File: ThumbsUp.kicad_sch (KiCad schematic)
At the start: 34 parts, among them J10 Raiser_Male, J13 Raiser_Female, J14 Raiser_Male, J17 Raiser_Female, J18 Raiser_Male, J19 Raiser_Female, J24 Conn_01x04_Male, J26 Conn_01x04_Male, J28 Conn_01x04_Female, J30 Conn_01x04_Female, J33 Raiser_Male, J34 Raiser_Female, J35 Raiser_Male, J38 Raiser_Female, J39 Raiser_Male, J40 Raiser_Female, J41 Raiser_Male, J47 Raiser_Female, J48 Raiser_Male, J9 Raiser_Female

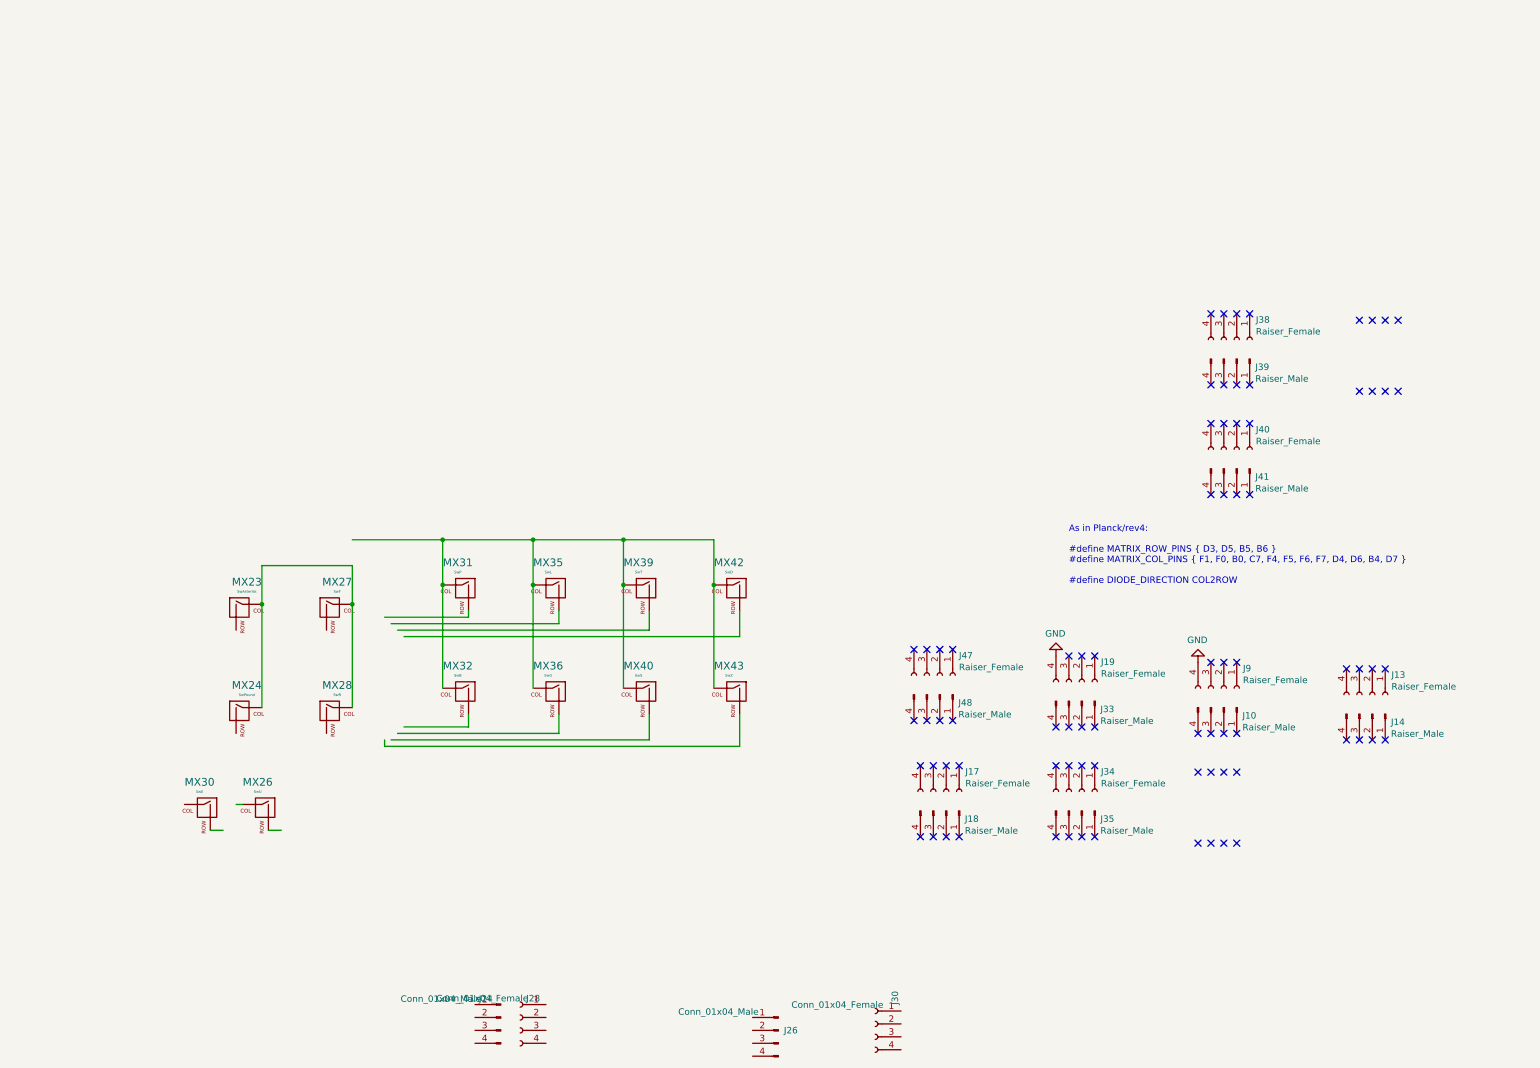
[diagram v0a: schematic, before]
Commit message: K12: Draft schematics, initial physical layout.
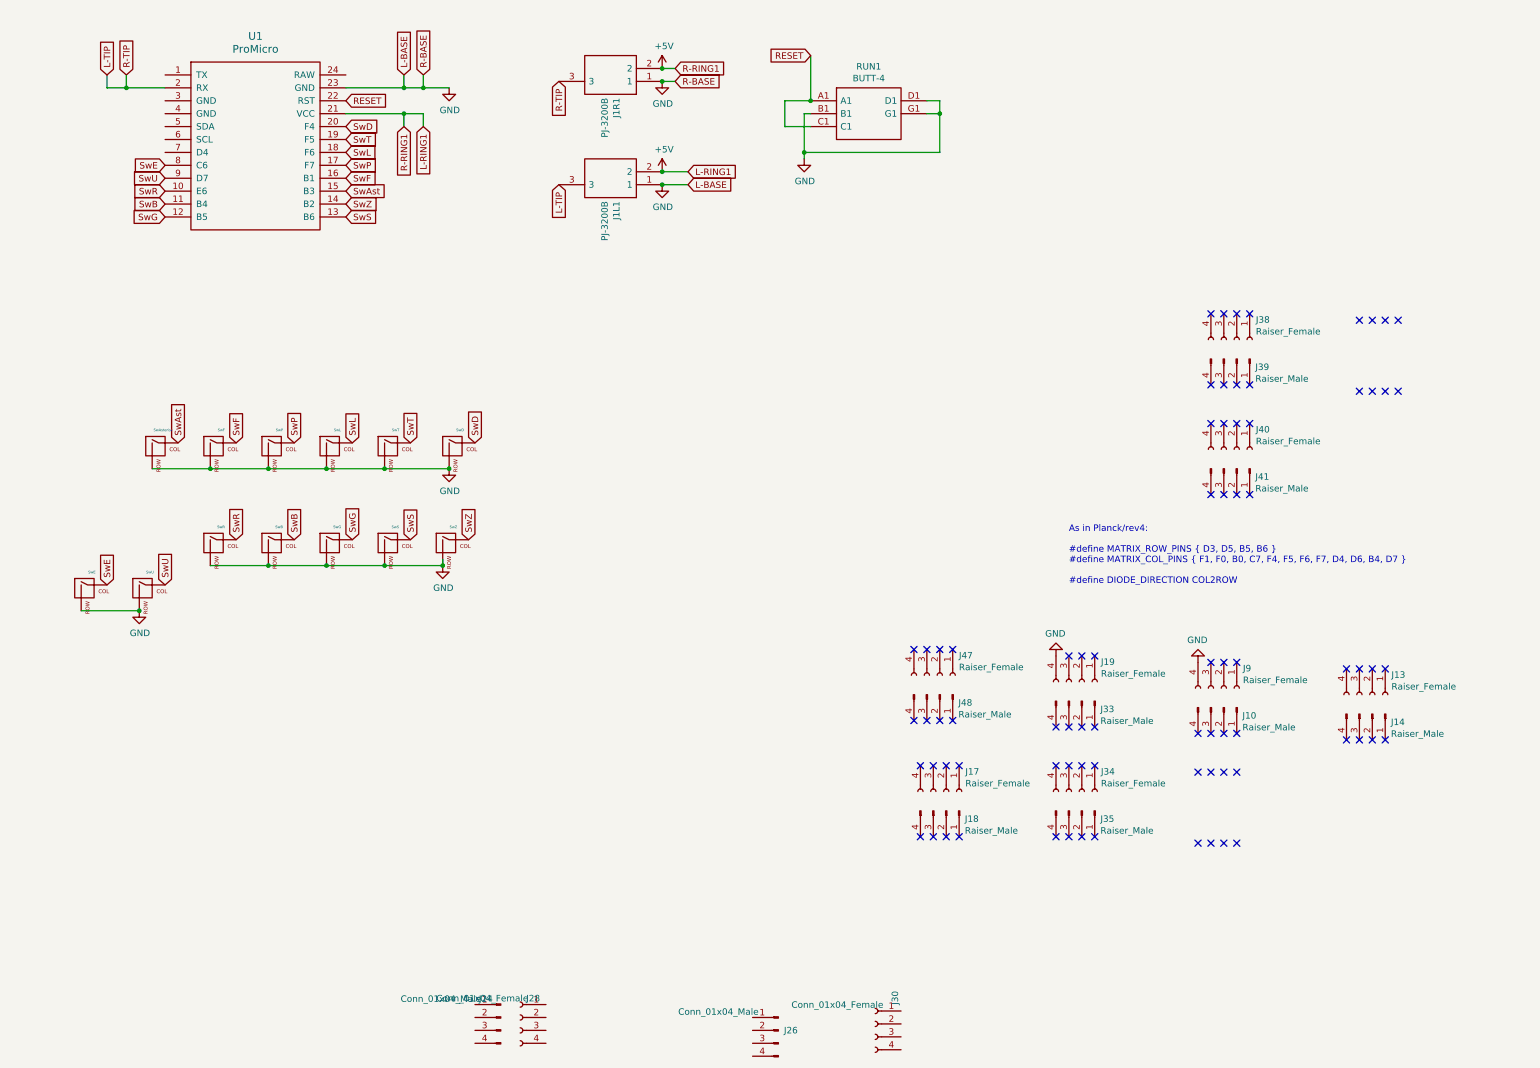
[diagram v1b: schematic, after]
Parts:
- removed MX24: SwPound, footprints:SW_D2FC_OMR, symbol ThumbsUp-rescue:MX-NoLED-MX_Alps_Hybrid
- added J1L1, J1R1: PJ-3200B, random-keyboard-parts:PJ-3200B-4A, symbol STX-3501-3N:STX-3501-3N
- added RUN1: BUTT-4, KiCad:BUTT4, symbol BUTT-4:BUTT-4
- added U1: ProMicro, promicro:ProMicro-NoSilk, symbol promicro:ProMicro
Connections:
- net GND: now also MX23.2 (ROW), MX26.2 (ROW), MX27.2 (ROW), MX28.2 (ROW), MX30.2 (ROW), MX31.2 (ROW), MX32.2 (ROW), MX35.2 (ROW), MX36.2 (ROW), MX39.2 (ROW), MX40.2 (ROW), MX42.2 (ROW), MX43.2 (ROW), J1L1.1, J1R1.1, RUN1.B1, RUN1.D1, RUN1.G1, U1.23 (GND)
- net SwE: now reaches MX30.1 (COL)
- net SwE: now also U1.8 (C6)
- net SwU: now reaches MX26.1 (COL)
- net SwU: now also U1.9 (D7)
- new net +5V: J1L1.2, J1R1.2, U1.21 (VCC)
- new net L-TIP: J1L1.3, J1R1.3, U1.2 (RX)
- new net RESET: RUN1.A1, RUN1.C1, U1.22 (RST)
- new net SwAst: MX23.1 (COL), U1.15 (B3)
- new net SwB: MX32.1 (COL), U1.11 (B4)
- new net SwD: MX42.1 (COL), U1.20 (F4)
- new net SwF: MX27.1 (COL), U1.16 (B1)
- new net SwG: MX36.1 (COL), U1.12 (B5)
- new net SwL: MX35.1 (COL), U1.18 (F6)
- new net SwP: MX31.1 (COL), U1.17 (F7)
- new net SwR: MX28.1 (COL), U1.10 (E6)
- new net SwS: MX40.1 (COL), U1.13 (B6)
- new net SwT: MX39.1 (COL), U1.19 (F5)
- new net SwZ: MX43.1 (COL), U1.14 (B2)

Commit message: K12: Before splitting the boards.
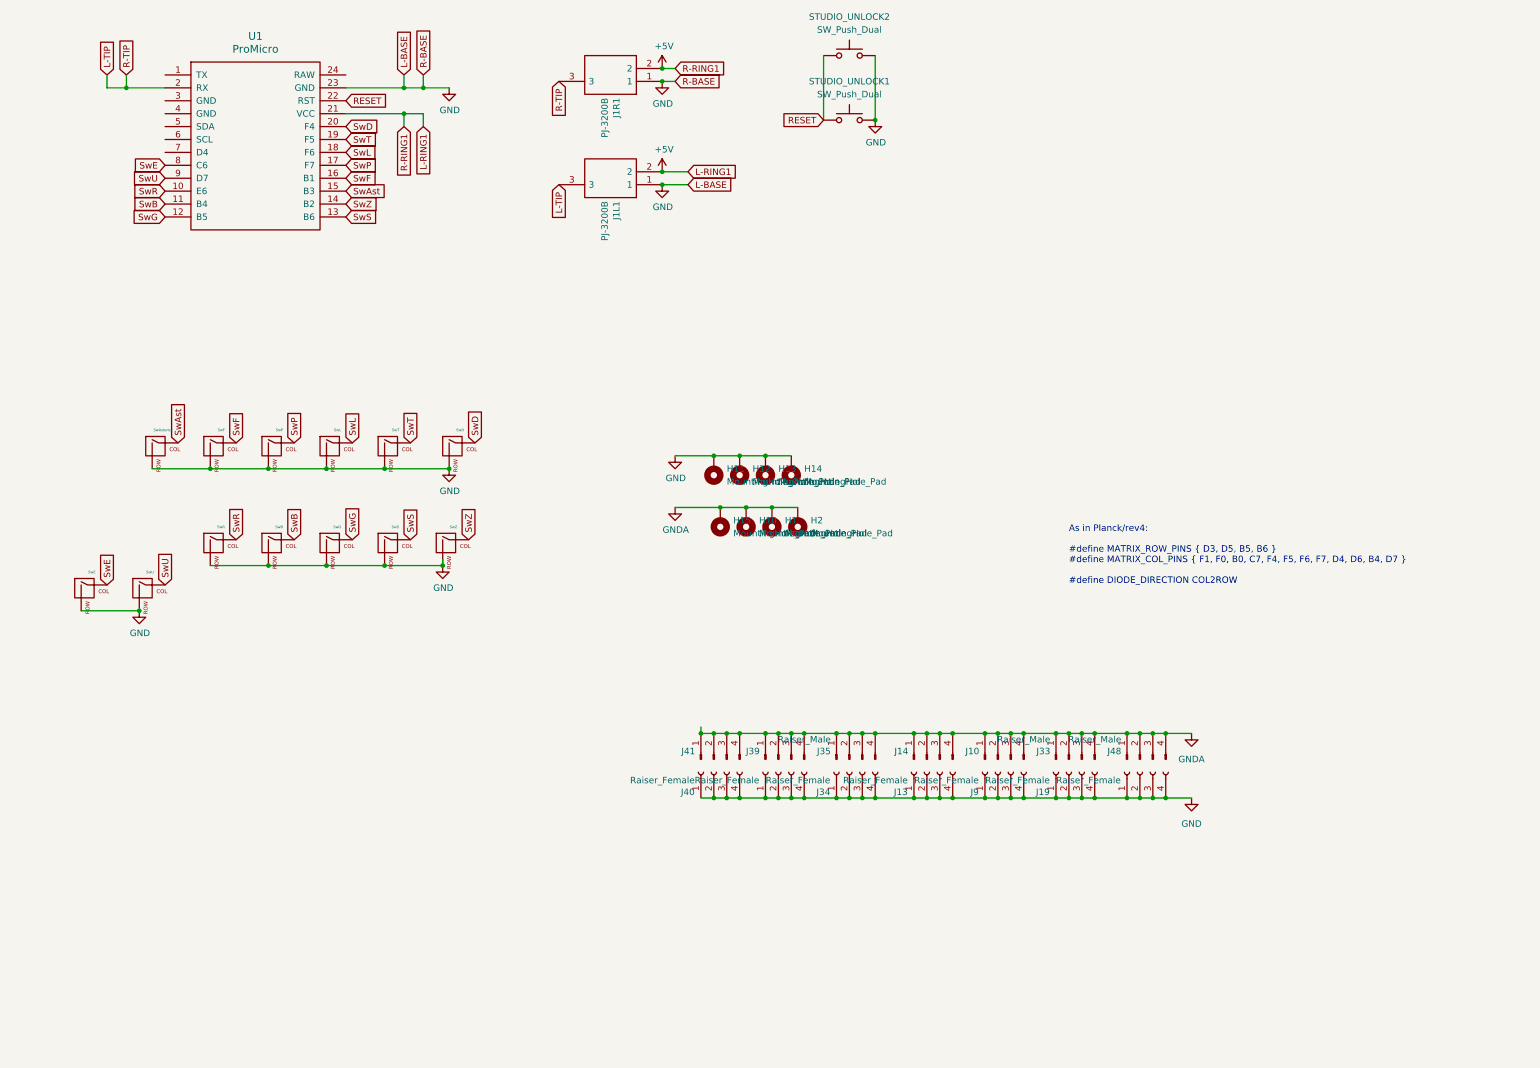
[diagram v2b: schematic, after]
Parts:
- removed J17: Raiser_Female, Connector_PinSocket_2.54mm:PinSocket_1x04_P2.54mm_Vertical, symbol Connector:Conn_01x04_Female
- removed J18: Raiser_Male, Connector_PinHeader_2.54mm:PinHeader_1x04_P2.54mm_Vertical, symbol Connector:Conn_01x04_Male
- removed J24, J26: Conn_01x04_Male, Connector_PinHeader_2.54mm:PinHeader_1x04_P2.54mm_Vertical, symbol Connector:Conn_01x04_Male
- removed J28, J30: Conn_01x04_Female, Connector_PinSocket_2.54mm:PinSocket_1x04_P2.54mm_Vertical, symbol Connector:Conn_01x04_Female
- removed RUN1: BUTT-4, KiCad:BUTT4, symbol BUTT-4:BUTT-4
- added H1, H10, H11, H12, H13, H14, H15, H2: MountingHole_Pad, MountingHole:MountingHole_3.5mm_Pad, symbol Mechanical:MountingHole_Pad
- added STUDIO_UNLOCK1, STUDIO_UNLOCK2: SW_Push_Dual, Button_Switch_SMD:SW_Push_1P1T_NO_CK_KSC6xxJ, symbol Switch:SW_Push
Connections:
- net GND: now also J13.1 (Pin_1), J13.2 (Pin_2), J13.3 (Pin_3), J13.4 (Pin_4), J19.1 (Pin_1), J19.2 (Pin_2), J19.3 (Pin_3), J34.1 (Pin_1), J34.2 (Pin_2), J34.3 (Pin_3), J34.4 (Pin_4), J38.1 (Pin_1), J38.2 (Pin_2), J38.3 (Pin_3), J38.4 (Pin_4), J40.1 (Pin_1), J40.2 (Pin_2), J40.3 (Pin_3), J40.4 (Pin_4), J47.1 (Pin_1), J47.2 (Pin_2), J47.3 (Pin_3), J47.4 (Pin_4), J9.1 (Pin_1), J9.2 (Pin_2), J9.3 (Pin_3), H11.1, H12.1, H13.1, H14.1, STUDIO_UNLOCK1.2, STUDIO_UNLOCK2.2
- net RESET: now also STUDIO_UNLOCK1.1, STUDIO_UNLOCK2.1
- net GNDA: now reaches J10.1 (Pin_1)
- net GNDA: now also J10.2 (Pin_2), J10.3 (Pin_3), J10.4 (Pin_4), J14.1 (Pin_1), J14.2 (Pin_2), J14.3 (Pin_3), J14.4 (Pin_4), J33.1 (Pin_1), J33.2 (Pin_2), J33.3 (Pin_3), J33.4 (Pin_4), J35.1 (Pin_1), J35.2 (Pin_2), J35.3 (Pin_3), J35.4 (Pin_4), J39.1 (Pin_1), J39.2 (Pin_2), J39.3 (Pin_3), J39.4 (Pin_4), J41.1 (Pin_1), J41.2 (Pin_2), J41.3 (Pin_3), J41.4 (Pin_4), J48.1 (Pin_1), J48.2 (Pin_2), J48.3 (Pin_3), J48.4 (Pin_4), H1.1, H10.1, H15.1, H2.1
- no-connect marks 78 -> 0
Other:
- moved on the sheet: J10, J13, J14, J19, J33, J34, J35, J39, J40, J41, J48, J9

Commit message: K12: Before generating Kerbers.
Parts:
- added H3: MountingHole_Pad, MountingHole:MountingHole_3.5mm_Pad, symbol Mechanical:MountingHole_Pad
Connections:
- new net GNDB: H3.1
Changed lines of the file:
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@@
 	)
 	(junction
+		(at 438.15 207.01)
+		(diameter 0)
+		(color 0 0 0 0)
+	)
+	(junction
 		(at 300.99 205.74)
 		(diameter 0)
@@
 	(wire
 		(pts
+			(xy 434.34 207.01) (xy 438.15 207.01)
+		)
+		(stroke
+			(width 0)
+			(type default)
+		)
+	)
+	(wire
+		(pts
 			(xy 505.46 345.44) (xy 510.54 345.44)
 		)
@@
 	(wire
 		(pts
+			(xy 425.45 302.26) (xy 416.56 302.26)
+		)
+		(stroke
+			(width 0)
+			(type default)
+		)
+	)
+	(wire
+		(pts
 			(xy 351.79 280.67) (xy 364.49 280.67)
 		)
@@
 	(wire
 		(pts
-			(xy 438.15 199.39) (xy 438.15 212.09)
+			(xy 438.15 199.39) (xy 438.15 207.01)
 		)
 		(stroke
@@
 	(wire
 		(pts
+			(xy 438.15 207.01) (xy 438.15 212.09)
+		)
+		(stroke
+			(width 0)
+			(type default)
+		)
+	)
+	(wire
+		(pts
 			(xy 474.98 345.44) (xy 477.52 345.44)
 		)
@@
 	(global_label "RESET"
 		(shape input)
-		(at 438.15 212.09 180)
+		(at 434.34 207.01 180)
 		(effects
 			(font
@@
 		)
 		(property "Intersheetrefs" "${INTERSHEET_REFS}"
-			(at 438.15 212.09 90)
+			(at 434.34 207.01 90)
 			(effects
 				(font
@@
 	(global_label "L-TIP"
 		(shape input)
-		(at 386.08 224.79 270)
+		(at 386.08 224.79 180)
 		(effects
 			(font
@@
 		)
 		(property "Intersheetrefs" "${INTERSHEET_REFS}"
-			(at 386.08 224.79 0)
+			(at 386.08 224.79 90)
 			(effects
 				(font
@@
 	(global_label "R-TIP"
 		(shape input)
-		(at 386.08 204.47 270)
+		(at 386.08 204.47 180)
 		(effects
 			(font
@@
 		)
 		(property "Intersheetrefs" "${INTERSHEET_REFS}"
-			(at 386.08 204.47 0)
+			(at 386.08 204.47 90)
 			(effects
 				(font
@@
 	(symbol
 		(lib_id "Mechanical:MountingHole_Pad")
+		(at 425.45 304.8 180)
+		(unit 1)
+		(exclude_from_sim no)
+		(in_bom no)
+		(on_board yes)
+		(dnp no)
+		(fields_autoplaced yes)
+		(property "Reference" "H3"
+			(at 427.99 304.7999 0)
+			(effects
+				(font
+					(size 1.27 1.27)
+				)
+				(justify right)
+			)
+		)
+		(property "Value" "MountingHole_Pad"
+			(at 427.99 307.3399 0)
+			(effects
+				(font
+					(size 1.27 1.27)
+				)
+				(justify right)
+			)
+		)
+		(property "Footprint" "MountingHole:MountingHole_3.5mm_Pad"
+			(at 425.45 304.8 0)
+			(effects
+				(font
+					(size 1.27 1.27)
+				)
+				(hide yes)
+			)
+		)
+		(property "Datasheet" "~"
+			(at 425.45 304.8 0)
+			(effects
+				(font
+					(size 1.27 1.27)
+				)
+				(hide yes)
+			)
+		)
+		(property "Description" "Mounting Hole with connection"
+			(at 425.45 304.8 0)
+			(effects
+				(font
+					(size 1.27 1.27)
+				)
+				(hide yes)
+			)
+		)
+		(pin "1"
+		)
+		(instances
+			(project "ThumbsUp"
+				(path "/467ed76c-995a-4514-a2e9-81ed0f98430e"
+					(reference "H3")
+					(unit 1)
+				)
+			)
+		)
+	)
+	(symbol
+		(lib_id "Mechanical:MountingHole_Pad")
 		(at 421.64 280.67 180)
 		(unit 1)
@@
 					(unit 1)
 				)
+			)
+		)
+	)
+	(symbol
+		(lib_id "power:GNDA")
+		(at 416.56 302.26 0)
+		(unit 1)
+		(exclude_from_sim no)
+		(in_bom yes)
+		(on_board yes)
+		(dnp no)
+		(property "Reference" "#PWR07"
+			(at 416.56 308.61 0)
+			(effects
+				(font
+					(size 1.27 1.27)
+				)
+				(hide yes)
+			)
+		)
+		(property "Value" "GNDB"
+			(at 416.687 306.6542 0)
+			(effects
+				(font
+					(size 1.27 1.27)
+				)
+			)
+		)
+		(property "Footprint" ""
+			(at 416.56 302.26 0)
+			(effects
+				(font
+					(size 1.27 1.27)
+				)
+				(hide yes)
+			)
+		)
+		(property "Datasheet" ""
+			(at 416.56 302.26 0)
+			(effects
+				(font
+					(size 1.27 1.27)
+				)
+				(hide yes)
+			)
+		)
+		(property "Description" ""
+			(at 416.56 302.26 0)
+			(effects
+				(font
+					(size 1.27 1.27)
+				)
+			)
+		)
+		(pin "1"
+		)
+		(instances
+			(project "ThumbsUp"
+				(path "/467ed76c-995a-4514-a2e9-81ed0f98430e"
+					(reference "#PWR07")
+					(unit 1)
+				)

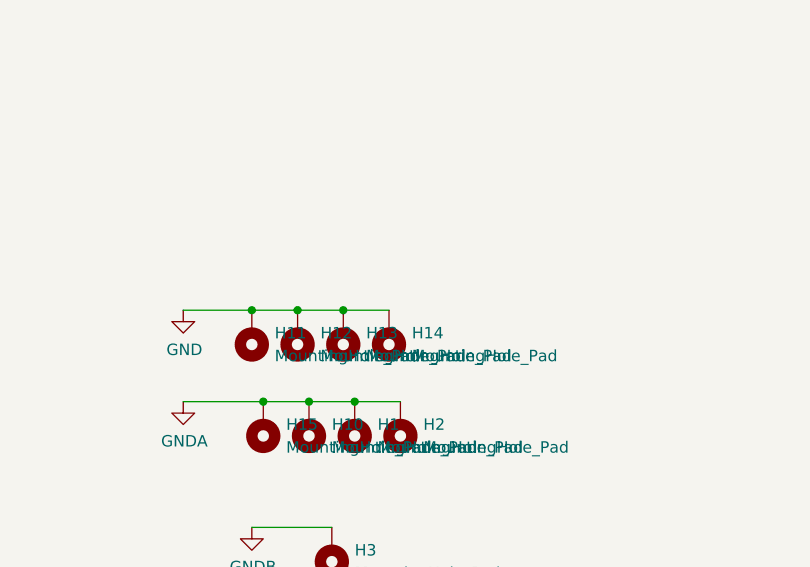
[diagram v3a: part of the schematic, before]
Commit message: K12: Added a mounting hole. Moved the tracks a bit. Haven't modified the gerbers
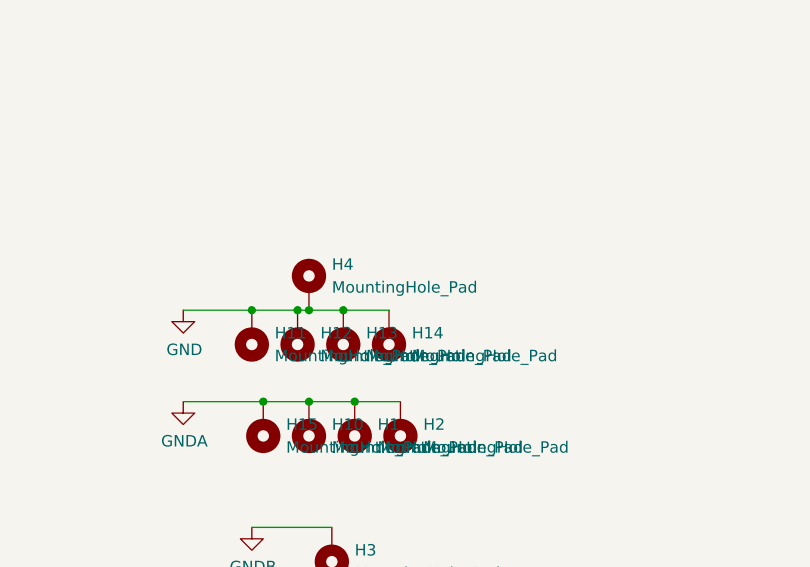
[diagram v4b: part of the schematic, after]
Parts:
- added H4: MountingHole_Pad, MountingHole:MountingHole_4.5mm_Pad, symbol Mechanical:MountingHole_Pad
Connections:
- net GND: now also H4.1
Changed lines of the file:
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@@
 	)
 	(junction
+		(at 422.91 278.13)
+		(diameter 0)
+		(color 0 0 0 0)
+	)
+	(junction
 		(at 491.49 345.44)
 		(diameter 0)
@@
 	(wire
 		(pts
+			(xy 422.91 278.13) (xy 426.72 278.13)
+		)
+		(stroke
+			(width 0)
+			(type default)
+		)
+	)
+	(wire
+		(pts
 			(xy 297.18 203.2) (xy 297.18 205.74)
 		)
@@
 	(wire
 		(pts
-			(xy 421.64 278.13) (xy 426.72 278.13)
+			(xy 421.64 278.13) (xy 422.91 278.13)
 		)
 		(stroke
@@
 					(unit 1)
 				)
+			)
+		)
+	)
+	(symbol
+		(lib_id "Mechanical:MountingHole_Pad")
+		(at 422.91 275.59 0)
+		(unit 1)
+		(exclude_from_sim no)
+		(in_bom no)
+		(on_board yes)
+		(dnp no)
+		(fields_autoplaced yes)
+		(property "Reference" "H4"
+			(at 425.45 273.0499 0)
+			(effects
+				(font
+					(size 1.27 1.27)
+				)
+				(justify left)
+			)
+		)
+		(property "Value" "MountingHole_Pad"
+			(at 425.45 275.5899 0)
+			(effects
+				(font
+					(size 1.27 1.27)
+				)
+				(justify left)
+			)
+		)
+		(property "Footprint" "MountingHole:MountingHole_4.5mm_Pad"
+			(at 422.91 275.59 0)
+			(effects
+				(font
+					(size 1.27 1.27)
+				)
+				(hide yes)
+			)
+		)
+		(property "Datasheet" "~"
+			(at 422.91 275.59 0)
+			(effects
+				(font
+					(size 1.27 1.27)
+				)
+				(hide yes)
+			)
+		)
+		(property "Description" "Mounting Hole with connection"
+			(at 422.91 275.59 0)
+			(effects
+				(font
+					(size 1.27 1.27)
+				)
+				(hide yes)
+			)
+		)
+		(pin "1"
+		)
+		(instances
+			(project ""
+				(path "/467ed76c-995a-4514-a2e9-81ed0f98430e"
+					(reference "H4")
+					(unit 1)
+				)
